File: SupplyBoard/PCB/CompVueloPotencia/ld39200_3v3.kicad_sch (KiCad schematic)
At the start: 7 parts, among them U2 LD39200DPUR

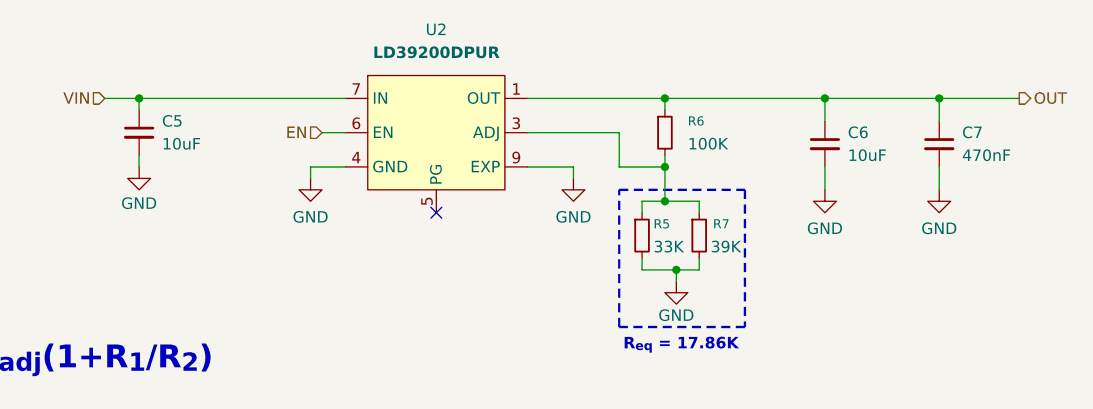
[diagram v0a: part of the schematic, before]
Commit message: SupplyBoard - finish current sense
Finish the Current Sensor Circuit and add more 3.3V out, i change de microcontroles to a mcu that have the exact GPIO's
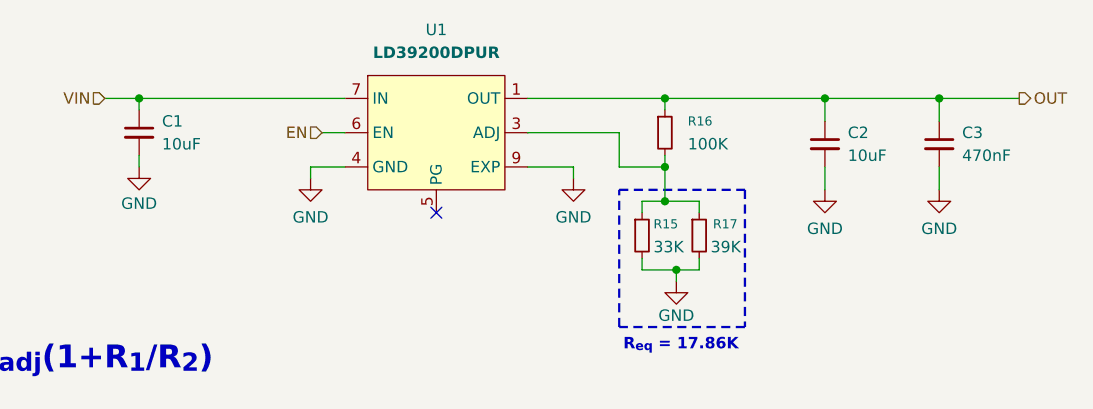
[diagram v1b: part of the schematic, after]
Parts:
- renumbered C5 to C1, C6 to C2, C7 to C3, R5 to R15, R6 to R16, R7 to R17, U2 to U1

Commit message: SupplyBoard - update layout
schematic completed and PCB layout started; only the routing of the traces remains to be done
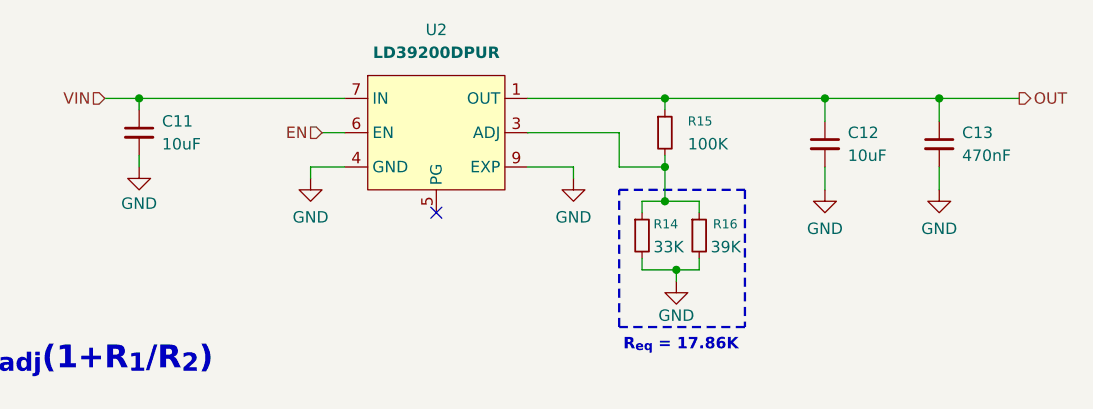
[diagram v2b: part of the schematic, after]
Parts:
- C11: renamed from C1; footprint (none) -> Capacitor_SMD:C_0805_2012Metric_Pad1.18x1.45mm_HandSolder
- C12: renamed from C2; footprint (none) -> Capacitor_SMD:C_0805_2012Metric_Pad1.18x1.45mm_HandSolder
- C13: renamed from C3; footprint (none) -> Capacitor_SMD:C_0805_2012Metric_Pad1.18x1.45mm_HandSolder
- R14: renamed from R15; footprint (none) -> Resistor_SMD:R_0805_2012Metric_Pad1.20x1.40mm_HandSolder
- R15: renamed from R16; footprint (none) -> Resistor_SMD:R_0805_2012Metric_Pad1.20x1.40mm_HandSolder
- R16: renamed from R17; footprint (none) -> Resistor_SMD:R_0805_2012Metric_Pad1.20x1.40mm_HandSolder
- renumbered U1 to U2
